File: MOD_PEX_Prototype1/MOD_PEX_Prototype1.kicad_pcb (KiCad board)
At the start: 2 copper layers, 78.4 x 40 mm, 70 parts, among them CN1 CONN_PANNEL_2X2, CN2 CONN_PANNEL_2X2, J1 RJ45_CHAIN_MAIN, J2 RJ45_CHAIN_EXTENSION, P1 HEADER_3X1, P2 HEADER_5X2, P3 HEADER_5X2, P4 HEADER_2X1, Q1 MMBT3904, Q2 MMBT3906, SW1 SWITCH_HH, U1 LPC111X_LQFP48, U2 AP1117E50G, U3 AP1117E33G, U4 MAX13450E, X1 10MHz

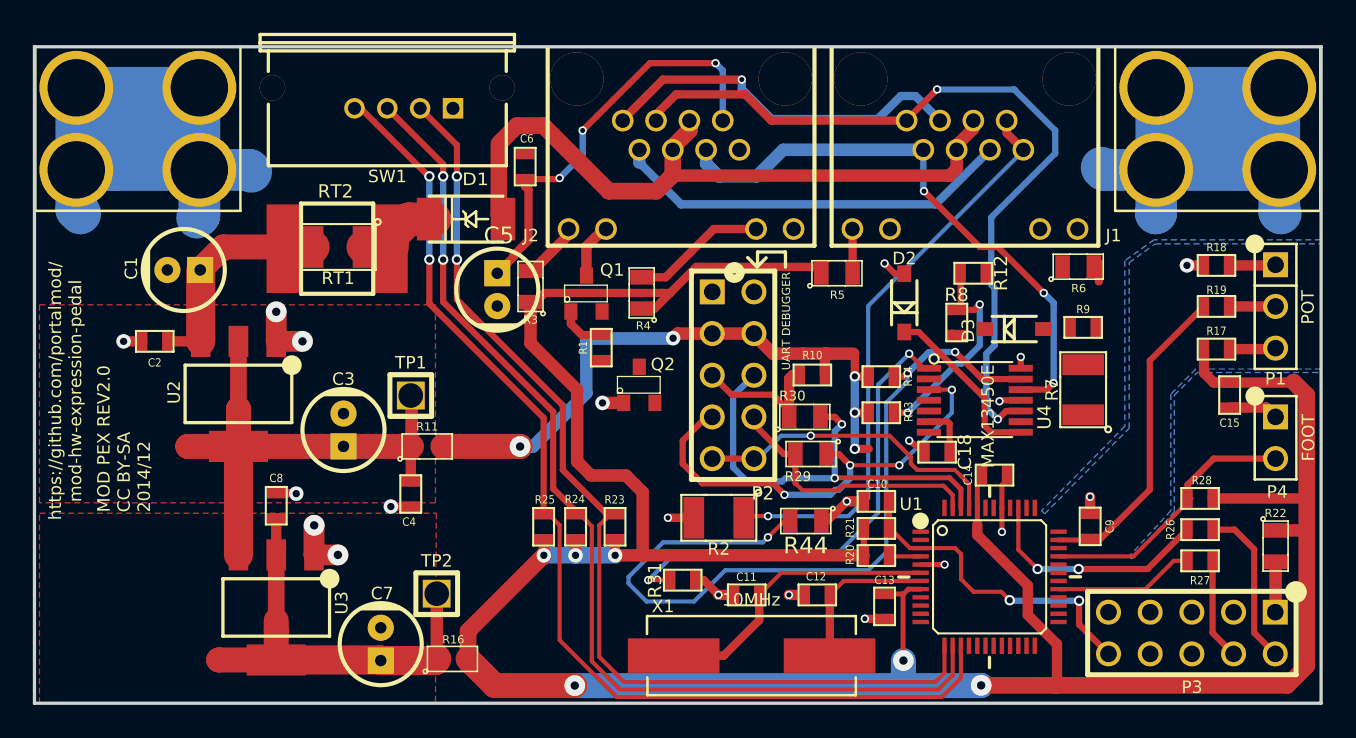
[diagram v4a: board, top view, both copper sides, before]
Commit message: fix issue #11 (new control chain circuitry): tracing the PCB to incorporate schematics changes.
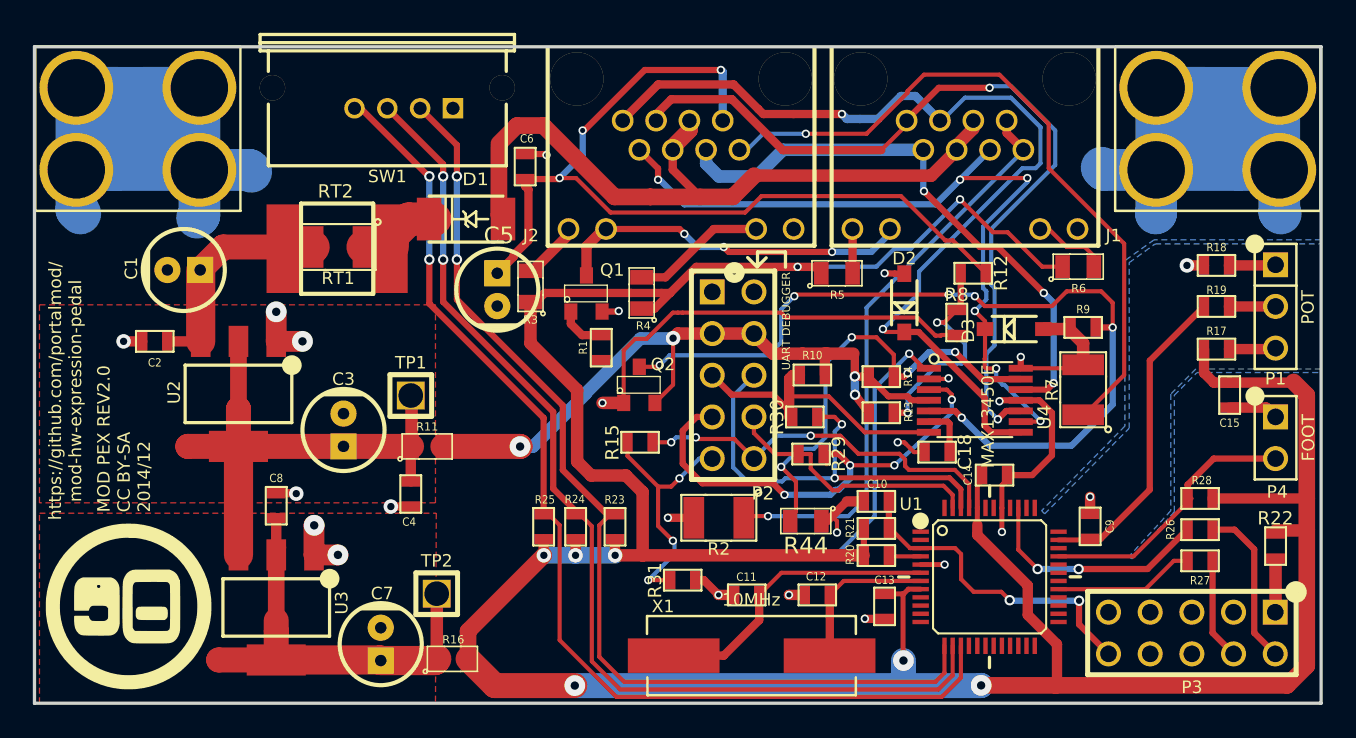
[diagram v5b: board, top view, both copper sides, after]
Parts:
- added G***: LOGO, MOD_Footprints_Lib:MOD_Logo, F.Cu at (69.2, 97.6)
- added R15: 0R, MOD_Footprints_Lib:SM0603, F.Cu at (100.4, 87.6)
- R22, R29, R30: footprint MOD_Footprints_Lib:SM0805 -> MOD_Footprints_Lib:SM0603
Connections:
- P2 pad 10: EN_CHAIN -> Net-(P2-Pad10)
- P2 pad 9: EN_CHAIN -> ENABLE_CHAIN
- R31 pad 1: TX_CHAIN_EN -> ENABLE_CHAIN
- U1 pad 45: EN_CHAIN -> Net-(P2-Pad10)
- U4 pad 1: TX_CHAIN_EN -> ENABLE_CHAIN
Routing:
- net RTERM_CHAIN: track 0.00 -> 53.1 mm, vias 0 -> 6
- net Net-(J2-Pad8): track 0.00 -> 42.8 mm, vias 0 -> 1
- net ENABLE_CHAIN: track 0.00 -> 41.1 mm, vias 0 -> 4
- net TX_CHAIN_EN: track 29.1 -> 0.00 mm, vias 2 -> 0
- net Net-(C5-Pad1): track 25.7 -> 54.5 mm
- net Net-(Q2-Pad1): track 1.69 -> 26.7 mm
- net RS485_RX+: track 33.6 -> 58.5 mm, vias 1 -> 2
- net RS485_RX-: track 24.7 -> 48.5 mm, vias 0 -> 6
- net Net-(P2-Pad10): track 0.00 -> 23.4 mm, vias 0 -> 3
- net Net-(R14-Pad2): track 49.8 -> 27.7 mm, vias 3 -> 4
- net DGND: track 151.0 -> 173.1 mm, vias 20 -> 23
- net +3.3V: track 180.3 -> 199.9 mm, vias 6 -> 8
- net EN_CHAIN: track 19.1 -> 0.00 mm, vias 1 -> 0
- net Net-(J1-Pad10): track 3.43 -> 22.0 mm, vias 0 -> 3
- net RX_CHAIN: track 9.04 -> 18.5 mm
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
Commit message: fixing footprint and labels positioning.
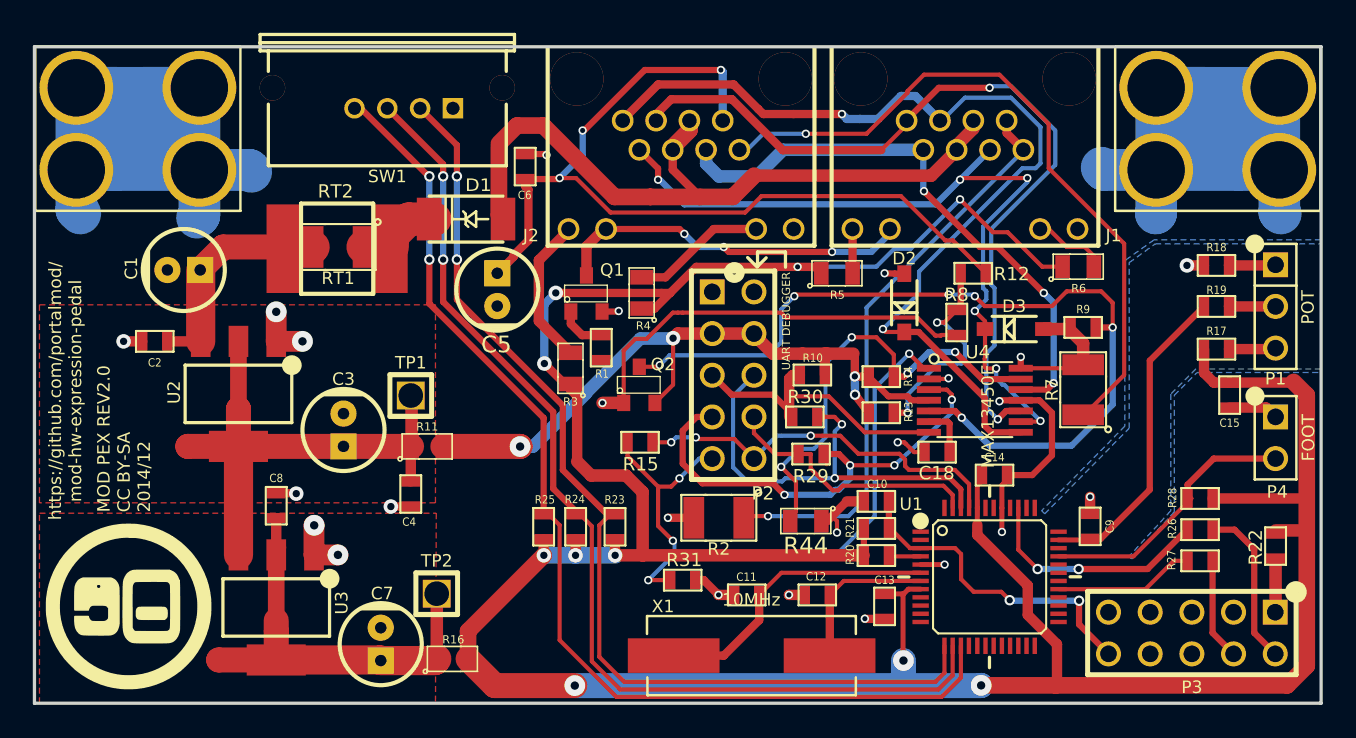
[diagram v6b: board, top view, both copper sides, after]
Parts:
- moved R3 5.55 mm to (96.2, 83.1)
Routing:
- net Net-(J2-Pad9): track 3.58 -> 9.44 mm
- net +3.3V: track 199.9 -> 198.8 mm, vias 8 -> 10
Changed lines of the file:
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@@
     (thickness 1.6)
     (drawings 23)
-    (tracks 839)
+    (tracks 846)
     (zones 0)
     (modules 72)
@@
   )
   (setup
-    (last_trace_width 0.254)
+    (last_trace_width 0.508)
     (user_trace_width 0.3048)
     (user_trace_width 0.381)
@@
     (at 93.4 70.8 90)
     (attr smd)
-    (fp_text reference C6 (at 1.7 0.1 180) (layer F.SilkS)
+    (fp_text reference C6 (at -1.7424 -0.0296 180) (layer F.SilkS)
       (effects (font (size 0.508 0.4572) (thickness 0.1143)))
     )
@@
     (at 122 89.6)
     (attr smd)
-    (fp_text reference C14 (at -1.6167 0.008 90) (layer F.SilkS)
+    (fp_text reference C14 (at 0.00128 -1.081 180) (layer F.SilkS)
       (effects (font (size 0.508 0.4572) (thickness 0.1143)))
     )
@@
     (tags "DO-214AC SMA")
     (attr smd)
-    (fp_text reference D1 (at -0.5732 2.4228 180) (layer F.SilkS)
+    (fp_text reference D1 (at -0.751 2.0672 180) (layer F.SilkS)
       (effects (font (size 0.762 0.8382) (thickness 0.1524)))
     )
@@
   (module MOD_Footprints_Lib:SOD123 (layer F.Cu)
     (at 123.2 80.7)
-    (fp_text reference D3 (at -2.8 0.1 90) (layer F.SilkS)
+    (fp_text reference D3 (at -0.00746 -1.39104 180) (layer F.SilkS)
       (effects (font (size 0.762 0.762) (thickness 0.1524)))
     )
@@
     (at 98.035 81.834 90)
     (attr smd)
-    (fp_text reference R1 (at 0 -1.1 90) (layer F.SilkS)
+    (fp_text reference R1 (at -1.59738 0.04964 360) (layer F.SilkS)
       (effects (font (size 0.508 0.4572) (thickness 0.1143)))
     )
@@
   )
   (module MOD_Footprints_Lib:SM0805 (layer F.Cu)
-    (at 93.726 78.105 90)
+    (at 96.16186 83.0961 90)
     (attr smd)
     (fp_text reference R3 (at -2.032 0 180) (layer F.SilkS)
@@
     (at 110.9 83.5 180)
     (attr smd)
-    (fp_text reference R10 (at 0 1.2 180) (layer F.SilkS)
+    (fp_text reference R10 (at -0.02434 1.03636 180) (layer F.SilkS)
       (effects (font (size 0.508 0.4572) (thickness 0.1143)))
     )
@@
     (at 134.5248 92.9226)
     (attr smd)
-    (fp_text reference R26 (at -1.8 0 90) (layer F.SilkS)
+    (fp_text reference R26 (at -1.6955 -0.06528 90) (layer F.SilkS)
       (effects (font (size 0.508 0.4572) (thickness 0.1143)))
     )
@@
     (at 134.5248 94.8226)
     (attr smd)
-    (fp_text reference R27 (at 0 1.2) (layer F.SilkS)
+    (fp_text reference R27 (at -1.74122 -0.04504 90) (layer F.SilkS)
       (effects (font (size 0.508 0.4572) (thickness 0.1143)))
     )
@@
     (at 134.5248 91.0226 180)
     (attr smd)
-    (fp_text reference R28 (at -0.1 1.1 180) (layer F.SilkS)
+    (fp_text reference R28 (at 1.68534 0.0398 270) (layer F.SilkS)
       (effects (font (size 0.508 0.4572) (thickness 0.1143)))
     )
@@
     (at 91.7 78.3)
     (attr smd)
-    (fp_text reference C5 (at 0.1 -3.3) (layer F.SilkS)
+    (fp_text reference C5 (at -0.05426 3.34576) (layer F.SilkS)
       (effects (font (size 1.016 1.016) (thickness 0.1524)))
     )
@@
     (at 118.5 88.2 180)
     (attr smd)
-    (fp_text reference C18 (at -1.6891 0.0127 270) (layer F.SilkS)
+    (fp_text reference C18 (at 0.02932 -1.27912 360) (layer F.SilkS)
       (effects (font (size 0.8128 0.8128) (thickness 0.1524)))
     )
@@
     (at 120.7 77.3 180)
     (attr smd)
-    (fp_text reference R12 (at -1.6891 0.0127 270) (layer F.SilkS)
+    (fp_text reference R12 (at -2.34268 -0.04808 360) (layer F.SilkS)
       (effects (font (size 0.8128 0.8128) (thickness 0.1524)))
     )
@@
     (at 103 96)
     (attr smd)
-    (fp_text reference R31 (at -1.6891 0.0127 90) (layer F.SilkS)
+    (fp_text reference R31 (at 0.08844 -1.2326 180) (layer F.SilkS)
       (effects (font (size 0.8128 0.8128) (thickness 0.1524)))
     )
@@
     (descr TSSOP-14)
     (attr smd)
-    (fp_text reference U4 (at 1.0686 -4.2418 270) (layer F.SilkS)
+    (fp_text reference U4 (at -2.89196 -0.17512 360) (layer F.SilkS)
       (effects (font (size 0.8128 0.8128) (thickness 0.1524)))
     )
@@
     (at 100.4 87.6)
     (attr smd)
-    (fp_text reference R15 (at -1.6891 0.0127 90) (layer F.SilkS)
+    (fp_text reference R15 (at 0.03668 1.3381 180) (layer F.SilkS)
       (effects (font (size 0.8128 0.8128) (thickness 0.1524)))
     )
@@
     (at 139.1248 93.9226 270)
     (attr smd)
-    (fp_text reference R22 (at -1.6891 0.0127 360) (layer F.SilkS)
+    (fp_text reference R22 (at 0.07772 1.21042 450) (layer F.SilkS)
       (effects (font (size 0.8128 0.8128) (thickness 0.1524)))
     )
@@
     (at 110.8202 88.3158 180)
     (attr smd)
-    (fp_text reference R29 (at -1.6891 0.0127 270) (layer F.SilkS)
+    (fp_text reference R29 (at 0.01524 -1.34874 360) (layer F.SilkS)
       (effects (font (size 0.8128 0.8128) (thickness 0.1524)))
     )
@@
     (at 110.4392 86.0552)
     (attr smd)
-    (fp_text reference R30 (at -1.6891 0.0127 90) (layer F.SilkS)
+    (fp_text reference R30 (at 0.03048 -1.22428 180) (layer F.SilkS)
       (effects (font (size 0.8128 0.8128) (thickness 0.1524)))
     )
@@
   (gr_line (start 141.9 103.5) (end 141.9 63.5) (angle 90) (layer Edge.Cuts) (width 0.2))
   (gr_line (start 63.5 63.5) (end 63.5 103.5) (angle 90) (layer Edge.Cuts) (width 0.2))
+  (segment (start 99.8474 78.5) (end 95.26654 78.5) (width 0.508) (layer F.Cu) (net 1))
+  (segment (start 101.3206 78.5) (end 99.8474 78.5) (width 0.508) (layer F.Cu) (net 1))
+  (segment (start 102.23878 78.5) (end 101.7016 78.5) (width 0.508) (layer F.Cu) (net 1))
+  (segment (start 101.7016 78.5) (end 101.3206 78.5) (width 0.508) (layer F.Cu) (net 1))
+  (segment (start 94.57182 82.80146) (end 95.81896 84.0486) (width 0.508) (layer F.Cu) (net 1))
+  (via (at 94.57182 82.80146) (size 0.889) (layers F.Cu B.Cu) (net 1))
+  (segment (start 94.57182 79.19212) (end 94.57182 82.80146) (width 0.508) (layer B.Cu) (net 1))
+  (segment (start 95.26524 78.4987) (end 94.57182 79.19212) (width 0.508) (layer B.Cu) (net 1))
+  (via (at 95.26524 78.4987) (size 0.889) (layers F.Cu B.Cu) (net 1))
+  (segment (start 95.26654 78.5) (end 95.26524 78.4987) (width 0.508) (layer F.Cu) (net 1))
+  (segment (start 95.81896 84.0486) (end 96.16186 84.0486) (width 0.508) (layer F.Cu) (net 1))
+  (segment (start 96.16186 84.0486) (end 96.16186 84.33816) (width 0.635) (layer F.Cu) (net 1))
+  (segment (start 96.16186 84.33816) (end 96.568106 84.744406) (width 0.635) (layer F.Cu) (net 1))
+  (segment (start 96.568106 84.744406) (end 96.568106 88.771712) (width 0.635) (layer F.Cu) (net 1))
   (via (at 110 76.9112) (size 0.508) (drill 0.3048) (layers F.Cu B.Cu) (net 1))
   (segment (start 126.1475 76.9) (end 124.9 76.9) (width 0.254) (layer F.Cu) (net 1))
@@
   (segment (start 100.5586 94.488) (end 114.026 94.488) (width 0.762) (layer F.Cu) (net 1))
   (segment (start 98.8822 94.488) (end 100.5586 94.488) (width 0.762) (layer F.Cu) (net 1))
-  (segment (start 96.568106 84.410906) (end 96.568106 88.771712) (width 0.762) (layer F.Cu) (net 1))
-  (segment (start 96.568106 84.410906) (end 93.726 81.5688) (width 0.762) (layer F.Cu) (net 1))
-  (segment (start 93.726 81.5688) (end 93.726 79.0575) (width 0.762) (layer F.Cu) (net 1))
   (segment (start 99.5426 89.624) (end 100.5586 90.64) (width 0.762) (layer F.Cu) (net 1))
   (segment (start 97.420394 89.624) (end 99.5426 89.624) (width 0.762) (layer F.Cu) (net 1))
@@
   (segment (start 116.425 100.875) (end 116.45 100.9) (width 0.3048) (layer F.Cu) (net 1))
   (segment (start 116.45 100.9) (end 116.45 102.425) (width 1.524) (layer B.Cu) (net 1))
-  (segment (start 93.726 79.0575) (end 94.0425 79.0575) (width 0.508) (layer F.Cu) (net 1))
-  (segment (start 94.0425 79.0575) (end 94.6 78.5) (width 0.508) (layer F.Cu) (net 1))
-  (segment (start 94.6 78.5) (end 99.8474 78.5) (width 0.508) (layer F.Cu) (net 1))
-  (segment (start 101.7016 78.5) (end 101.3206 78.5) (width 0.508) (layer F.Cu) (net 1))
   (segment (start 102.23878 78.5) (end 103.82758 76.9112) (width 0.508) (layer F.Cu) (net 1))
-  (segment (start 102.23878 78.5) (end 101.7016 78.5) (width 0.508) (layer F.Cu) (net 1))
-  (segment (start 101.3206 78.5) (end 99.8474 78.5) (width 0.508) (layer F.Cu) (net 1))
   (segment (start 111.4475 77.3) (end 111.0587 76.9112) (width 0.508) (layer F.Cu) (net 1))
   (segment (start 103.82758 76.9112) (end 110 76.9112) (width 0.508) (layer F.Cu) (net 1))
@@
   (segment (start 125.304 74.604) (end 126.4 75.7) (width 0.254) (layer F.Cu) (net 25))
   (segment (start 124.772 74.604) (end 125.304 74.604) (width 0.254) (layer F.Cu) (net 25))
-  (segment (start 93.8475 77.1525) (end 96.042 74.958) (width 0.635) (layer F.Cu) (net 26))
+  (segment (start 96.042 74.604) (end 96.042 74.6968) (width 0.254) (layer F.Cu) (net 26))
+  (segment (start 96.042 74.6968) (end 94.234 76.5048) (width 0.635) (layer F.Cu) (net 26))
+  (segment (start 94.234 80.21574) (end 96.16186 82.1436) (width 0.635) (layer F.Cu) (net 26))
+  (segment (start 94.234 76.5048) (end 94.234 80.21574) (width 0.635) (layer F.Cu) (net 26))
   (segment (start 96.042 74.958) (end 96.042 74.604) (width 0.635) (layer F.Cu) (net 26))
-  (segment (start 93.726 77.1525) (end 93.8475 77.1525) (width 0.635) (layer F.Cu) (net 26))
   (segment (start 101.9525 77.5475) (end 104.896 74.604) (width 0.508) (layer F.Cu) (net 27))
   (segment (start 104.896 74.604) (end 107.472 74.604) (width 0.508) (layer F.Cu) (net 27))
